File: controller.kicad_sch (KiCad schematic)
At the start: 6 parts, among them U1 ESP32-C6-DevKitC-1

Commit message: Initial routing
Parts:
- added Brd1: SSD1306, SSD1306:128x64OLED, symbol SSD1306-128x64_OLED:SSD1306
- added J1: Barrel_Jack_MountingPin, Connector_BarrelJack:BarrelJack_CUI_PJ-063AH_Horizontal, symbol Connector:Barrel_Jack_MountingPin
- added J2: Conn_01x02_Pin, Connector_Molex:Molex_SL_171971-0002_1x02_P2.54mm_Vertical, symbol Connector:Conn_01x02_Pin
- added J3: Conn_01x07_Pin, Connector_Molex:Molex_SL_171971-0007_1x07_P2.54mm_Vertical, symbol Connector:Conn_01x07_Pin
- added J4: Screw_Terminal_01x06, TerminalBlock_RND:TerminalBlock_RND_205-00005_1x06_P5.00mm_Horizontal, symbol Connector:Screw_Terminal_01x06
- added JP1: SolderJumper_3_Bridged12, Jumper:SolderJumper-3_P1.3mm_Open_RoundedPad1.0x1.5mm_NumberLabels, symbol Jumper:SolderJumper_3_Bridged12
- added LED_POWER1: LED, LED_SMD:LED_0805_2012Metric_Pad1.15x1.40mm_HandSolder, symbol Device:LED
- added Q1, Q2, Q3, Q4, Q5: IRLTS6342TRPBF, Package_SO:TSOP-6_1.65x3.05mm_P0.95mm, symbol controller_library:IRLTS6342TRPBF
- added R1, R2, R3, R4, R5, R6: 15k, Resistor_SMD:R_0603_1608Metric_Pad0.98x0.95mm_HandSolder, symbol Device:R
- added RoutSMD1, RoutSMD2, RoutSMD3, RoutSMD4, RoutSMD5: 0, Resistor_SMD:R_0805_2012Metric_Pad1.20x1.40mm_HandSolder, symbol Device:R
- added RoutTH1, RoutTH2, RoutTH3, RoutTH4, RoutTH5: 0, Resistor_THT:R_Axial_DIN0204_L3.6mm_D1.6mm_P5.08mm_Horizontal, symbol Device:R
- LED1: renamed from D1; footprint (none) -> LED_SMD:LED_0805_2012Metric_Pad1.15x1.40mm_HandSolder
- LED2: renamed from D2; footprint (none) -> LED_SMD:LED_0805_2012Metric_Pad1.15x1.40mm_HandSolder
- LED3: renamed from D3; footprint (none) -> LED_SMD:LED_0805_2012Metric_Pad1.15x1.40mm_HandSolder
- LED4: renamed from D4; footprint (none) -> LED_SMD:LED_0805_2012Metric_Pad1.15x1.40mm_HandSolder
- LED5: renamed from D5; footprint (none) -> LED_SMD:LED_0805_2012Metric_Pad1.15x1.40mm_HandSolder
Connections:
- net +3.3V: now reaches U1.1 (3V3)
- net +3.3V: now also Brd1.2 (VCC)
- net PWM4: now reaches U1.10 (GPIO10)
- net PWM4: now also J3.5 (Pin_5), Q4.3 (G), R4.2
- net PWM5: now reaches U1.11 (GPIO11)
- net PWM5: now also J3.6 (Pin_6), Q5.3 (G), R5.2
- net +5V: now reaches U1.14 (5V)
- net +5V: now also JP1.1 (A)
- net GND: now reaches U1.15 (GND)
- net GND: now also LED1.1 (K), LED2.1 (K), LED3.1 (K), LED4.1 (K), LED5.1 (K), U1.18 (GND), U1.21 (GND), U1.32 (GND), Brd1.1 (GND), J1.2, J2.2 (Pin_2), J3.1 (Pin_1), J3.7 (Pin_7), LED_POWER1.1 (K), Q1.4 (S), Q2.4 (S), Q3.4 (S), Q4.4 (S), Q5.4 (S)
- net PWM3: now reaches U1.26 (GPIO21)
- net PWM3: now also J3.4 (Pin_4), Q3.3 (G), R3.2
- net PWM2: now reaches U1.27 (GPIO22)
- net PWM2: now also J3.3 (Pin_3), Q2.3 (G), R2.2
- net PWM1: now reaches U1.28 (GPIO23)
- net PWM1: now also J3.2 (Pin_2), Q1.3 (G), R1.2
- net I2C_SDA: now reaches U1.5 (GPIO6)
- net I2C_SDA: now also Brd1.4 (SDA)
- net I2C_SCL: now reaches U1.6 (GPIO7)
- net I2C_SCL: now also Brd1.3 (SCL)
- net at LED2.2 (A): now also R2.1
- net at LED1.2 (A): now also R1.1
- net at LED3.2 (A): now also R3.1
- net at LED4.2 (A): now also R4.1
- net at LED5.2 (A): now also R5.1
- new net: Q4.1 (D), Q4.2 (D), Q4.5 (D), Q4.6 (D), RoutSMD4.2, RoutTH4.2
- new net: Q3.1 (D), Q3.2 (D), Q3.5 (D), Q3.6 (D), RoutSMD3.2, RoutTH3.2
- new net: J1.1, J2.1 (Pin_1), JP1.3 (B)
- new net: Q1.1 (D), Q1.2 (D), Q1.5 (D), Q1.6 (D), RoutSMD1.2, RoutTH1.2
- new net: Q5.1 (D), Q5.2 (D), Q5.5 (D), Q5.6 (D), RoutSMD5.2, RoutTH5.2
- new net: Q2.1 (D), Q2.2 (D), Q2.5 (D), Q2.6 (D), RoutSMD2.2, RoutTH2.2
- new net: LED_POWER1.2 (A), R6.2
- new net OUT1: J4.2 (Pin_2), RoutSMD1.1, RoutTH1.1
- new net OUT2: J4.3 (Pin_3), RoutSMD2.1, RoutTH2.1
- new net OUT3: J4.4 (Pin_4), RoutSMD3.1, RoutTH3.1
- new net OUT4: J4.5 (Pin_5), RoutSMD4.1, RoutTH4.1
- new net OUT5: J4.6 (Pin_6), RoutSMD5.1, RoutTH5.1
- new net VDD: J4.1 (Pin_1), JP1.2 (C), R6.1
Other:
- note added: "LED power supply"
- note added: "Optional Microcontroller"
- note added: "Optional Screen"
- moved on the sheet: LED1, LED2, LED3, LED4, LED5, U1

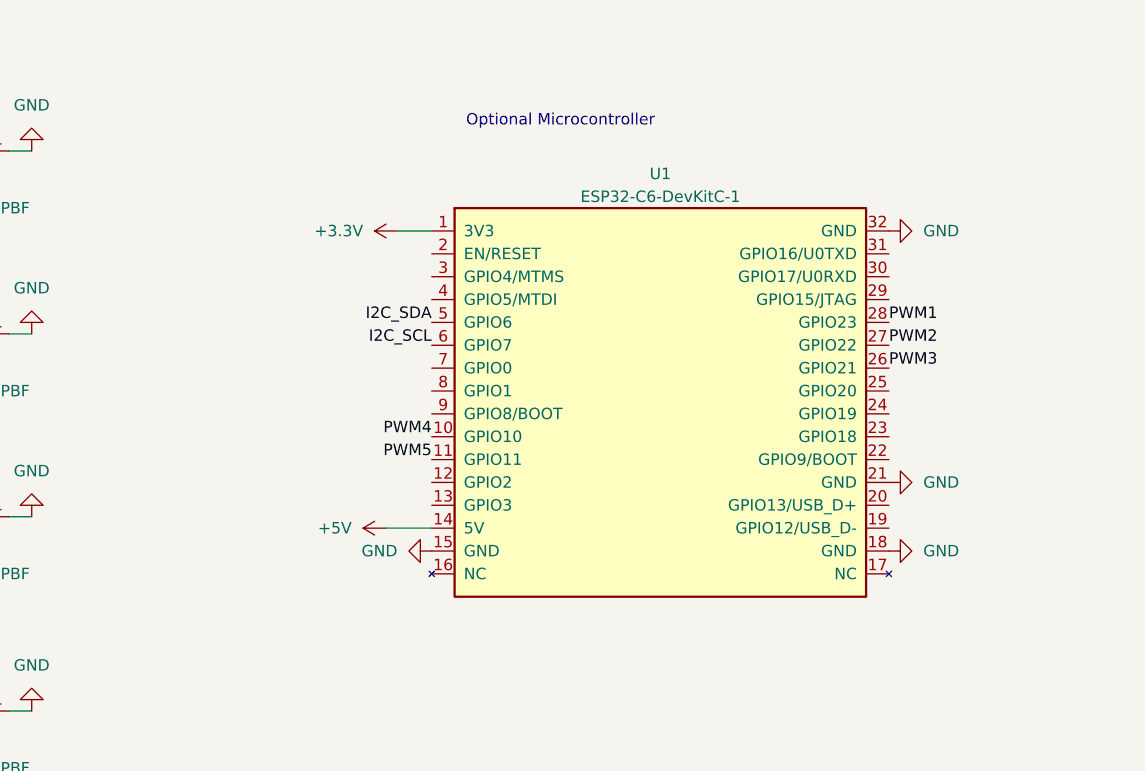
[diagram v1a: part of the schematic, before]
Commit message: Add button
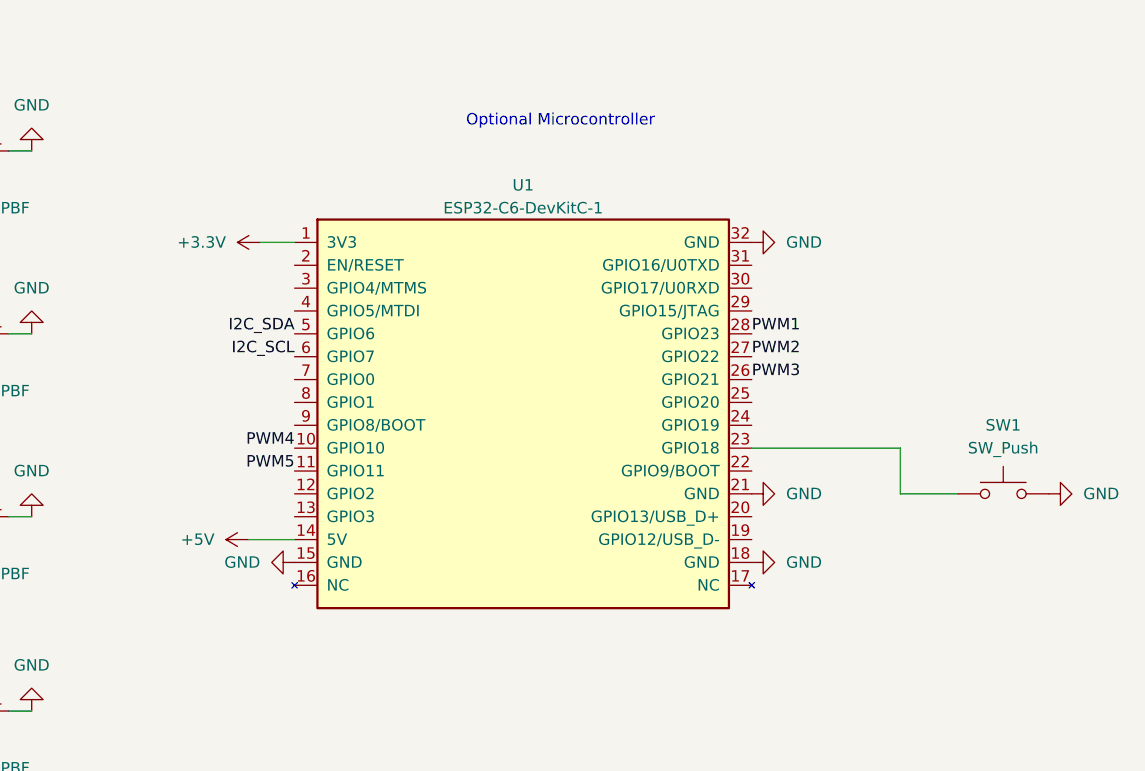
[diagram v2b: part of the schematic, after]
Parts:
- added SW1: SW_Push, symbol Switch:SW_Push
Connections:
- net GND: now also SW1.2
- net at U1.23 (GPIO18): now also SW1.1
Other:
- moved on the sheet: U1

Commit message: Commit unsaved changes
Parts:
- SW1: footprint (none) -> Button_Switch_SMD:SW_SPST_EVQP0
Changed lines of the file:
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@@
       (effects (font (size 1.27 1.27)))
     )
-    (property "Footprint" "" (at 269.24 96.52 0)
+    (property "Footprint" "Button_Switch_SMD:SW_SPST_EVQP0" (at 269.24 96.52 0)
       (effects (font (size 1.27 1.27)) hide)
     )

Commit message: Updates for PCB v2
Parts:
- removed RoutSMD1, RoutSMD2, RoutSMD3, RoutSMD4, RoutSMD5: 0, Resistor_SMD:R_0805_2012Metric_Pad1.20x1.40mm_HandSolder, symbol Device:R
- added C1: 100n, symbol Device:C
- added J5: Conn_01x03_Pin, symbol Connector:Conn_01x03_Pin
- added JP2: SolderJumper_3_Bridged12, Jumper:SolderJumper-3_P1.3mm_Open_RoundedPad1.0x1.5mm_NumberLabels, symbol Jumper:SolderJumper_3_Bridged12
- added JP3: SolderJumper_2_Bridged, symbol Jumper:SolderJumper_2_Bridged
- added JP4, JPout1, JPout2, JPout3, JPout4, JPout5: SolderJumper_2_Open, symbol Jumper:SolderJumper_2_Open
- added Rpd1, Rpd2, Rpd3, Rpd4, Rpd5: 100k, Resistor_SMD:R_0603_1608Metric_Pad0.98x0.95mm_HandSolder, symbol Device:R
- added VR1: Wurth Elektronik 1769405x41, controller_library:1769405x41, symbol controller_library:Wurth_Elektronik_1769405241
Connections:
- net +5V: now also JP2.1 (A), JP4.2 (B)
- net GND: now also C1.2, J5.1 (Pin_1), JP3.2 (B), Rpd1.1, Rpd2.1, Rpd3.1, Rpd4.1, Rpd5.1, VR1.4 (VOUT-); no longer Q1.4 (S), Q2.4 (S), Q3.4 (S), Q4.4 (S), Q5.4 (S)
- net OUT1: now also JPout1.1 (A), Rpd1.2
- net OUT2: now also JPout2.1 (A), Rpd2.2
- net OUT3: now also JPout3.1 (A), Rpd3.2
- net OUT4: now also JPout4.1 (A), Rpd4.2
- net OUT5: now also JPout5.1 (A), Rpd5.2
- net at Q4.1 (D), Q4.2 (D), Q4.5 (D)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: now also JPout4.2 (B)
- net ADDR_LED_OUT: now reaches U1.25 (GPIO20)
- net ADDR_LED_OUT: now also J5.2 (Pin_2)
- net at Q3.1 (D), Q3.2 (D), Q3.5 (D)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: now also JPout3.2 (B)
- net VIN: now reaches J1.1, J2.1 (Pin_1), JP1.3 (B)
- net VIN: now also C1.1, JP2.3 (B), VR1.2 (VIN+)
- net at Q1.1 (D), Q1.2 (D), Q1.5 (D)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: now also JPout1.2 (B)
- net at Q5.1 (D), Q5.2 (D), Q5.5 (D)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: now also JPout5.2 (B)
- net at Q2.1 (D), Q2.2 (D), Q2.5 (D)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: now also JPout2.2 (B)
- new net: J5.3 (Pin_3), JP2.2 (C)
- new net: JP4.1 (A), VR1.5 (VOUT+)
- new net GNDPWR: JP3.1 (A), Q1.4 (S), Q2.4 (S), Q3.4 (S), Q4.4 (S), Q5.4 (S), VR1.1 (VIN-)
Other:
- note added: "Addressable LED strip"
- note added: "External power supply"
- note added: "PWM connector"
- note added: "Pull-down resistors Optional, prevent unstable output during boot. You can also use 15k instead of 100k to reduce BOM"
- note added: "Star Ground to keep return paths in check"
- note removed: "LED power supply"
- moved on the sheet: J3, J4, LED1, LED2, LED3, LED4, LED5, LED_POWER1, Q1, Q2, Q3, Q4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

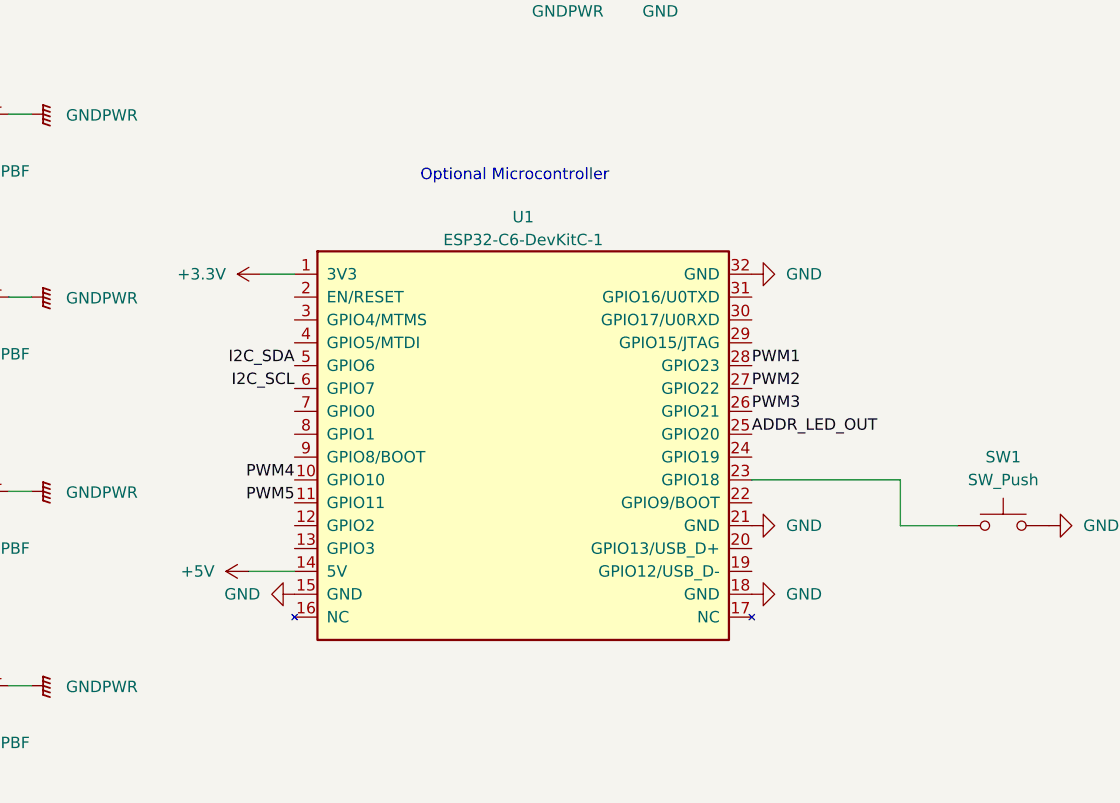
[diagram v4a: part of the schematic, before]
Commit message: Fix switch footprint
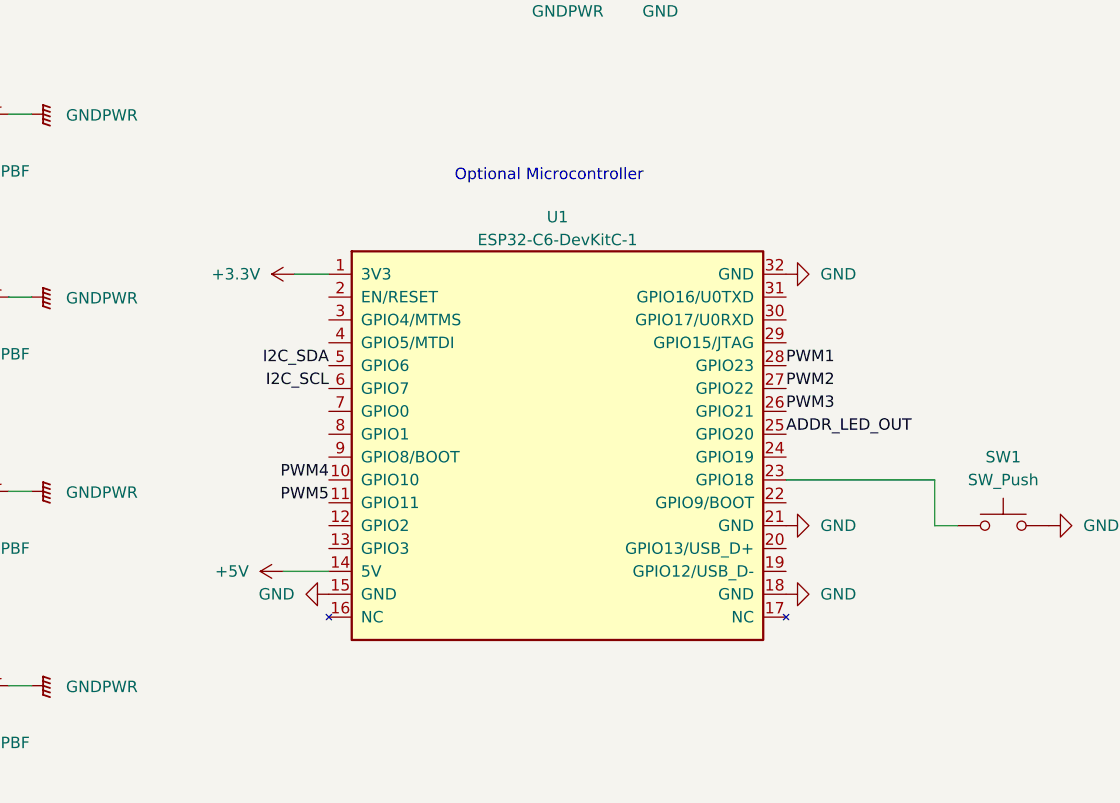
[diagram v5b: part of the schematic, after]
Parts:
- C1: footprint (none) -> Capacitor_SMD:C_0603_1608Metric_Pad1.08x0.95mm_HandSolder
- J5: footprint (none) -> Connector_Molex:Molex_SL_171971-0003_1x07_P2.54mm_Vertical
- JP3: footprint (none) -> Jumper:SolderJumper-2_P1.3mm_Bridged2Bar_Pad1.0x1.5mm
- JP4: footprint (none) -> Jumper:SolderJumper-2_P1.3mm_Open_RoundedPad1.0x1.5mm
- JPout1, JPout2, JPout3, JPout4, JPout5: footprint (none) -> Jumper:SolderJumper-2_P1.3mm_Open_TrianglePad1.0x1.5mm
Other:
- moved on the sheet: U1

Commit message: Complete routing
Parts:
- removed RoutTH1, RoutTH2, RoutTH3, RoutTH4, RoutTH5: 0, Resistor_THT:R_Axial_DIN0204_L3.6mm_D1.6mm_P5.08mm_Horizontal, symbol Device:R
- J1: footprint Connector_BarrelJack:BarrelJack_CUI_PJ-063AH_Horizontal -> Connector_BarrelJack:BarrelJack_CUI_PJ-063AH_Horizontal_CircularHoles
- J5: footprint Connector_Molex:Molex_SL_171971-0003_1x07_P2.54mm_Vertical -> Connector_Molex:Molex_SL_171971-0003_1x03_P2.54mm_Vertical
- SW1: footprint Button_Switch_SMD:SW_SPST_EVQP0 -> controller_library:SWITCH-4
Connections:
- net GND: no longer J1.2, J2.2 (Pin_2), LED_POWER1.1 (K)
- net GNDPWR: now also J1.2, J2.2 (Pin_2), LED_POWER1.1 (K)
- net OUT1: no longer Rpd1.2
- net OUT2: no longer Rpd2.2
- net OUT3: no longer Rpd3.2
- net OUT4: no longer Rpd4.2
- net OUT5: no longer Rpd5.2
- net PWM1: now also Rpd1.2
- net PWM2: now also Rpd2.2
- net PWM3: now also Rpd3.2
- net PWM4: now also Rpd4.2
- net PWM5: now also Rpd5.2
